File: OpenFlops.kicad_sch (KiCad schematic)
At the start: 87 parts, among them J99 OSHW_LOGO, P1 FLOPPY_CONN, P10 SD CARD, P11 SD PWR, P12 SD_DISABLE, P2 POWER_INPUT, P3 USB_A_FEMALE, P4 PROG_PORT, P5 JUMPER_JC, P6 ENCODER_PORT, P7 DISPLAY_PORT, P8 USB_HEADER, P9 EXTERNAL_SPEAKER, Q1 BSS138, Q2 BSS138, Q3 BSS138, Q4 BSS138, Q5 BSS138, Q6 BSS138, Q7 MMBT3904, U1 74HCT04, U3 STM32F105RBT6, U4 LM1117-3.3, Y1 8 MHz

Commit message: Change C1, C17 and C19 to SMD parts
This commit changes C1, C17 and C19 to SMD electrolytic capacitors. The Panasonic FT series (see https://industrial.panasonic.com/cdbs/www-data/pdf/RDE0000/ABA0000C1240.pdf) has both 10µF and 100µF available with 5x5.8 packages, so these are the used footprints.
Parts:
- C1, C17, C19: footprint Capacitor_THT:CP_Radial_D6.3mm_P2.50mm -> Capacitor_SMD:CP_Elec_5x5.8
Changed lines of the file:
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@@
 			)
 		)
-		(property "Footprint" "Capacitor_THT:CP_Radial_D6.3mm_P2.50mm"
+		(property "Footprint" "Capacitor_SMD:CP_Elec_5x5.8"
 			(at 138.303 56.388 0)
 			(effects
@@
 			)
 		)
-		(property "Description" ""
+		(property "Description" "Panasonic EEEFT1H100AR"
 			(at 138.303 56.388 0)
 			(effects
@@
 			)
 		)
-		(property "Footprint" "Capacitor_THT:CP_Radial_D6.3mm_P2.50mm"
+		(property "Footprint" "Capacitor_SMD:CP_Elec_5x5.8"
 			(at 170.18 56.388 0)
 			(effects
@@
 			)
 		)
-		(property "Description" ""
+		(property "Description" "Panasonic EEEFT1H100AR"
 			(at 170.18 56.388 0)
 			(effects
@@
 			)
 		)
-		(property "Footprint" "Capacitor_THT:CP_Radial_D6.3mm_P2.50mm"
+		(property "Footprint" "Capacitor_SMD:CP_Elec_5x5.8"
 			(at 114.808 55.753 0)
 			(effects
@@
 			)
 		)
-		(property "Description" ""
+		(property "Description" "Panasonic EEEFT1C101AR"
 			(at 114.808 55.753 0)
 			(effects

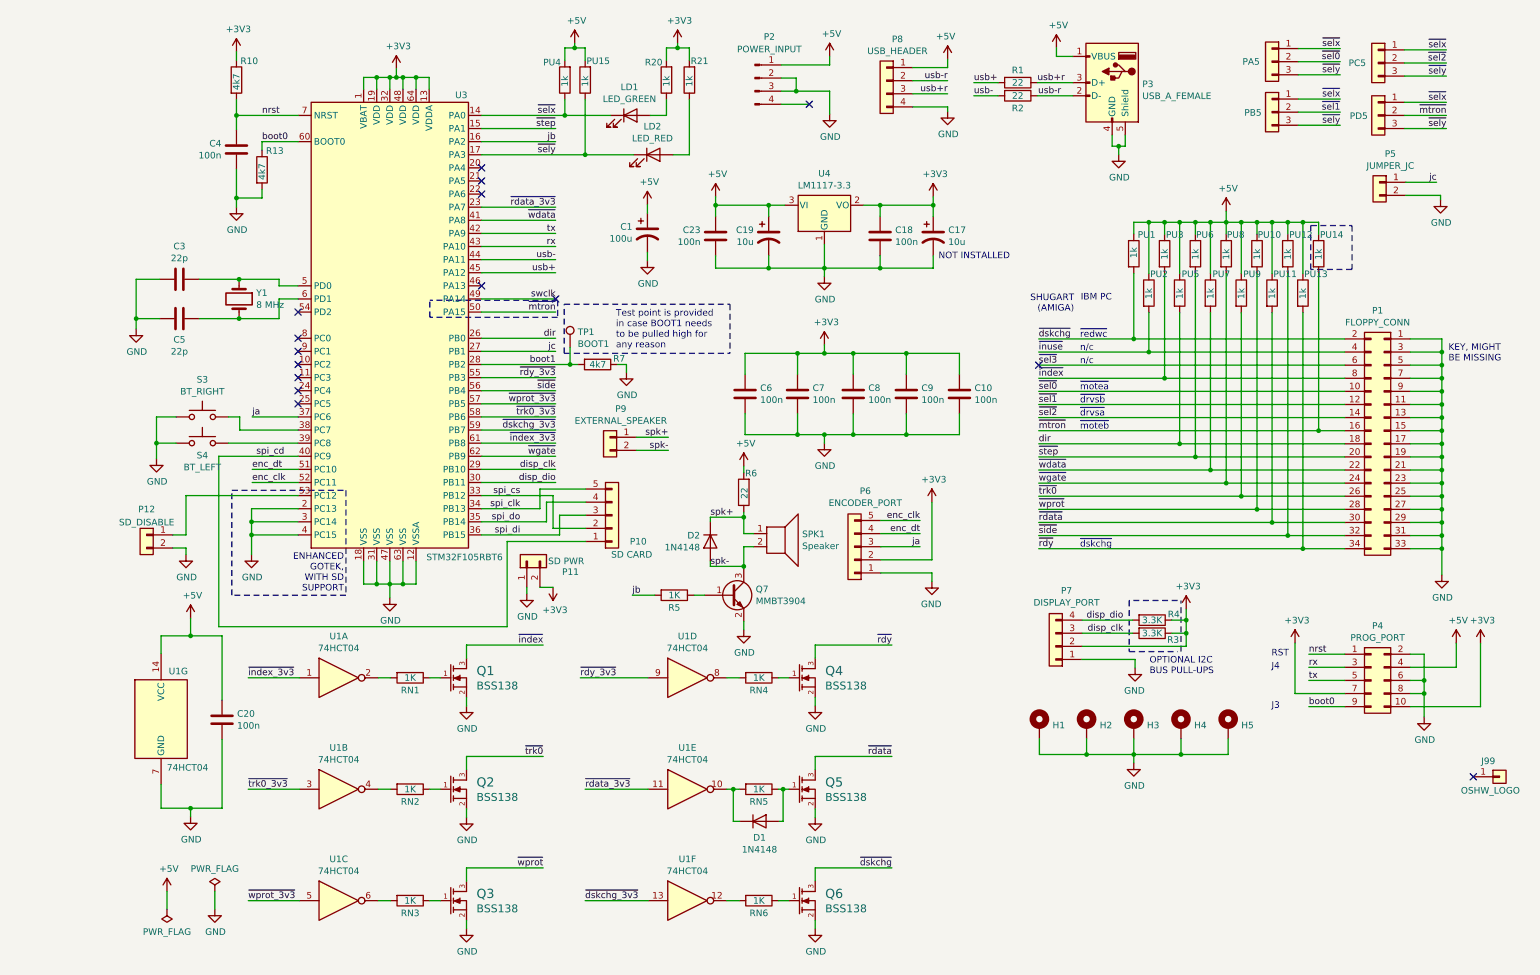
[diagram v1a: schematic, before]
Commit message: Major rerouting Still not completely satisfied though
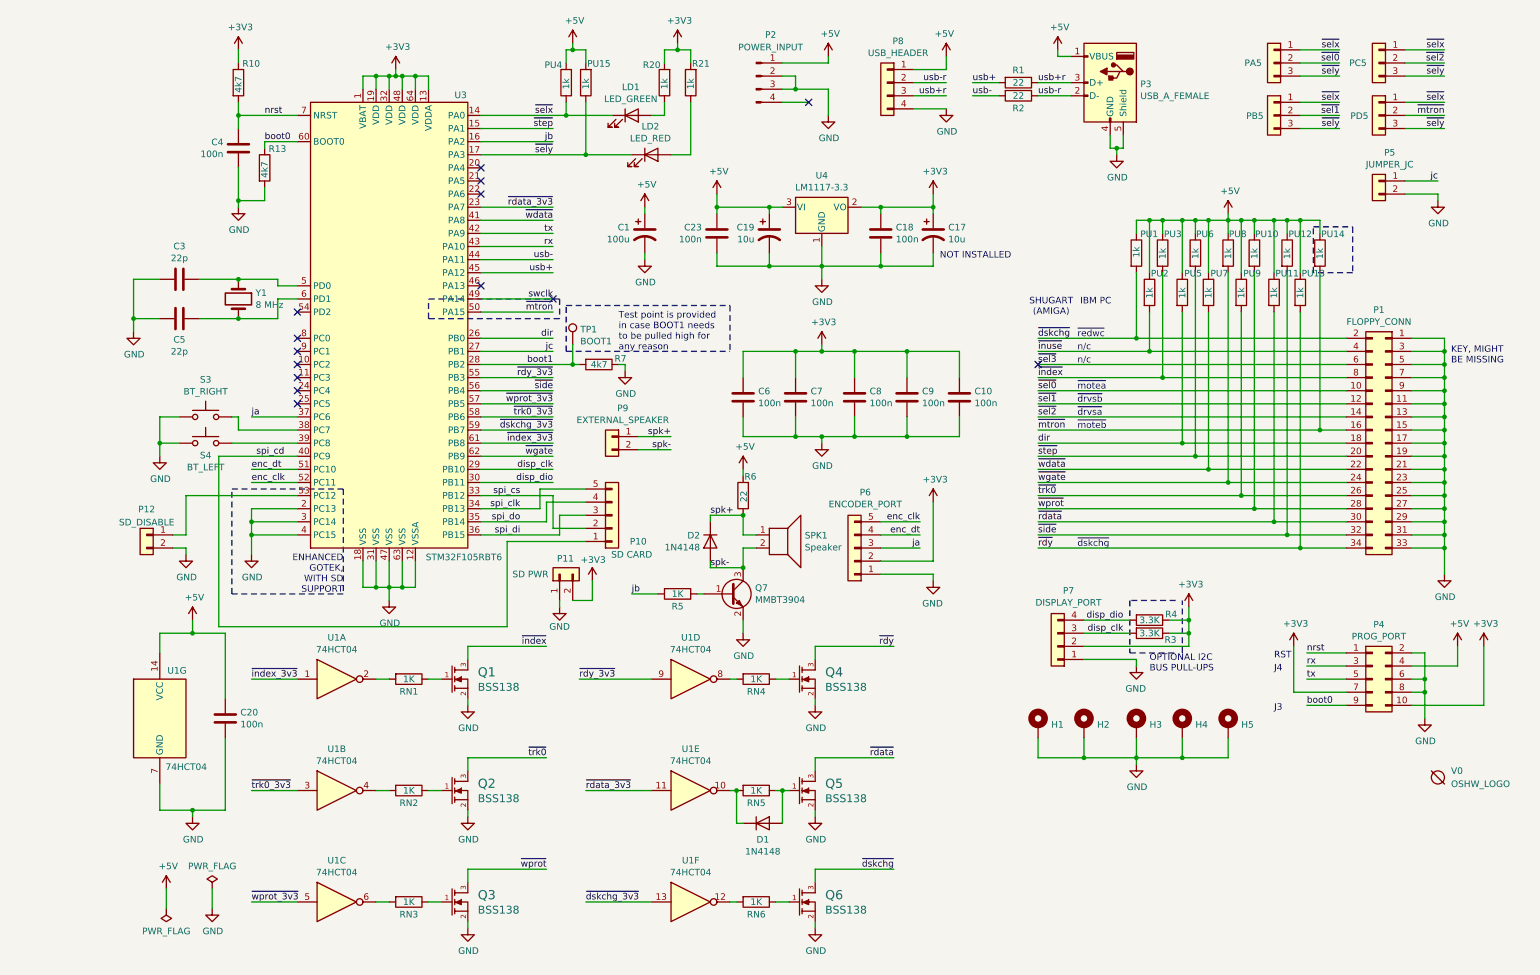
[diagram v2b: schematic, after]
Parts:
- removed J99: OSHW_LOGO, Symbol:OSHW-Logo2_9.8x8mm_Copper, symbol Connector_Generic:Conn_01x01
- added V0: OSHW_LOGO, Symbol:OSHW-Logo2_9.8x8mm_Copper, symbol void:Void
- Q7: footprint Package_TO_SOT_SMD:SOT-23_Handsoldering -> Package_TO_SOT_SMD:SOT-23
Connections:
- no-connect marks 15 -> 14
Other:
- moved on the sheet: C1, C10, C17, C18, C19, C20, C23, C6, C7, C8, C9, D1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

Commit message: Update footprints
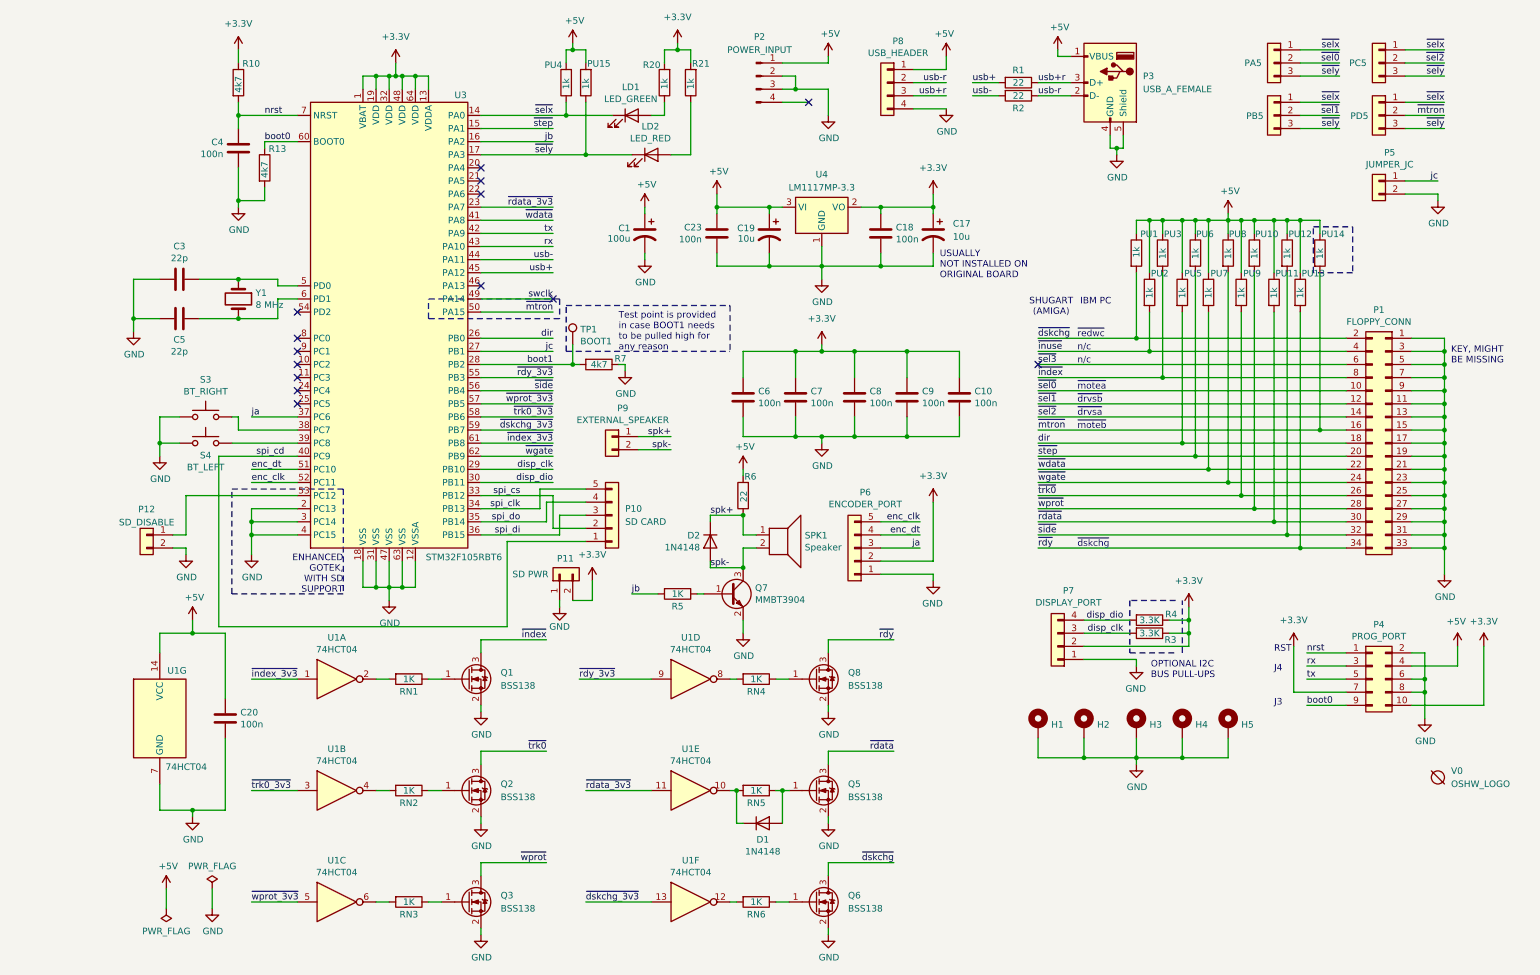
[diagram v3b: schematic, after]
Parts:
- removed C1: 100u, Capacitor_SMD:CP_Elec_5x5.8, symbol OpenFlops-rescue:CP1-Device
- removed C17, C19: 10u, Capacitor_SMD:CP_Elec_5x5.8, symbol OpenFlops-rescue:CP1-Device
- removed P2: POWER_INPUT, OpenFlops:PinHeader_1x04_P2.54mm_Vertical, symbol Connector:Conn_01x04_Male
- removed P3: USB_A_FEMALE, OpenFlops:USB_A_FEMALE, symbol OpenFlops-rescue:USB_A-Connector
- removed Q1, Q2, Q3, Q4, Q5, Q6: BSS138, Package_TO_SOT_SMD:SOT-23_Handsoldering, symbol OpenFlops-rescue:MOS_N_GSD-w_transistor
- removed U4: LM1117-3.3, Package_TO_SOT_SMD:SOT-223-3_TabPin2, symbol Regulator_Linear:LM1117-3.3
- added C1: 100u, Capacitor_SMD:CP_Elec_5x5.8, symbol Device:C_Polarized_US
- added C17, C19: 10u, Capacitor_SMD:CP_Elec_5x5.8, symbol Device:C_Polarized_US
- added P2: POWER_INPUT, Connector_PinHeader_2.54mm:PinHeader_1x04_P2.54mm_Vertical, symbol Connector:Conn_01x04_Pin
- added P3: USB_A_FEMALE, OpenFlops:USB_A_FEMALE, symbol Connector:USB_A
- added Q1, Q2, Q3, Q5, Q6, Q8: BSS138, Package_TO_SOT_SMD:SOT-23, symbol Transistor_FET:BSS138
- added U4: LM1117MP-3.3, Package_TO_SOT_SMD:SOT-223-3_TabPin2, symbol Regulator_Linear:LM1117MP-3.3
- C10, C18, C20, C23, C3, C4, C5, C6, C7, C8, C9: footprint Capacitor_SMD:C_0805_2012Metric_Pad1.15x1.40mm_HandSolder -> Capacitor_SMD:C_0805_2012Metric_Pad1.18x1.45mm_HandSolder
- P10, P6: footprint OpenFlops:PinHeader_1x05_P2.54mm_Vertical -> Connector_PinHeader_2.54mm:PinHeader_1x05_P2.54mm_Vertical
- P11, P12, P5: footprint OpenFlops:PinHeader_1x02_P2.54mm_Vertical -> Connector_PinHeader_2.54mm:PinHeader_1x02_P2.54mm_Vertical
- P4: footprint OpenFlops:PinHeader_2x05_P2.54mm_Vertical -> Connector_PinHeader_2.54mm:PinHeader_2x05_P2.54mm_Vertical
- P7, P8: footprint OpenFlops:PinHeader_1x04_P2.54mm_Vertical -> Connector_PinHeader_2.54mm:PinHeader_1x04_P2.54mm_Vertical
- PU1, PU10, PU11, PU12, PU13, PU14, PU15, PU2, PU3, PU4, PU5, PU6, PU7, PU8, PU9, R1, R10, R13, R2, R20, R21, R3, R4, R5, R6, R7, RN1, RN2, RN3, RN4, RN5, RN6: footprint Resistor_SMD:R_0805_2012Metric_Pad1.15x1.40mm_HandSolder -> Resistor_SMD:R_0805_2012Metric_Pad1.20x1.40mm_HandSolder
- V0: footprint Symbol:OSHW-Logo2_9.8x8mm_Copper -> Symbol:OSHW-Logo2_7.3x6mm_Copper
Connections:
- net +5V: now also C1.1, C19.1, P2.1 (Pin_1), P3.1 (VBUS), U4.3 (VI)
- net GND: now also C1.2, C17.2, C19.2, P2.2 (Pin_2), P2.3 (Pin_3), P3.4 (GND), P3.5 (Shield), Q1.2 (S), Q2.2 (S), Q3.2 (S), Q5.2 (S), Q6.2 (S), Q8.2 (S), U4.1 (GND)
- net usb+r: now also P3.3 (D+)
- net usb-r: now also P3.2 (D-)
- net ~{dskchg}: now also Q6.3 (D)
- net ~{index}: now also Q1.3 (D)
- net ~{rdata}: now also Q5.3 (D)
- net ~{rdy}: now also Q8.3 (D)
- net ~{trk0}: now also Q2.3 (D)
- net ~{wprot}: now also Q3.3 (D)
- net at RN1.1: now also Q1.1 (G)
- net at RN2.1: now also Q2.1 (G)
- net at RN3.1: now also Q3.1 (G)
- net at RN4.1: now also Q8.1 (G)
- net at D1.2 (A), RN5.1: now also Q5.1 (G)
- net at RN6.1: now also Q6.1 (G)
- net +3V3 renamed +3.3V
- net +3.3V: now also C17.1, U4.2 (VO)
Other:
- note added: "USUALLY NOT INSTALLED ON ORIGINAL BOARD"
- note removed: "NOT INSTALLED"

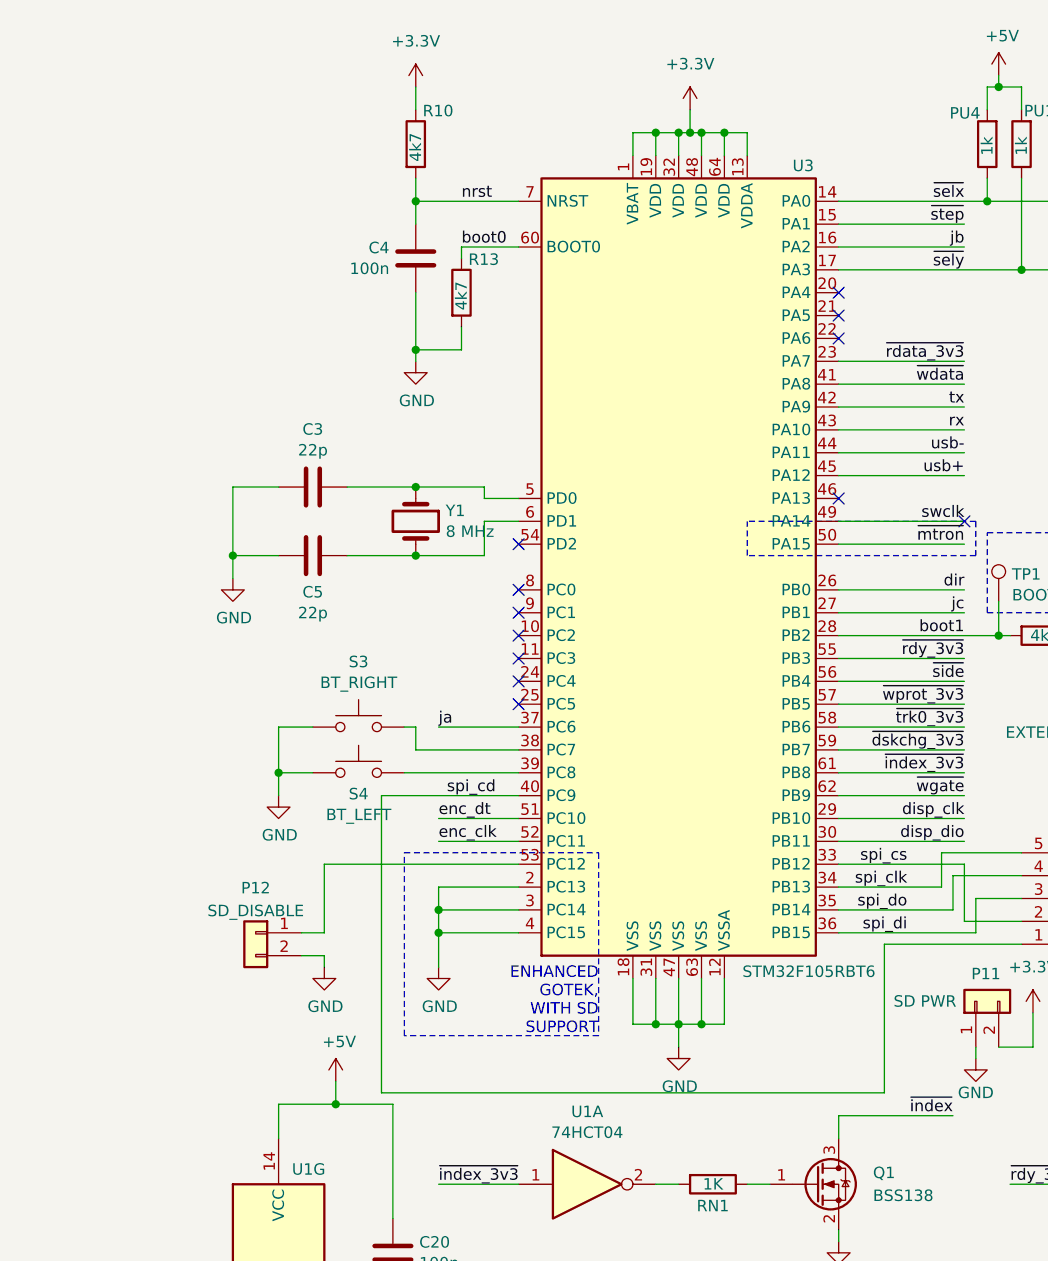
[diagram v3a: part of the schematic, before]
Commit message: Update MCU footprint MCU and MOSFET are no longer "handsolder", not sure if it's OK...
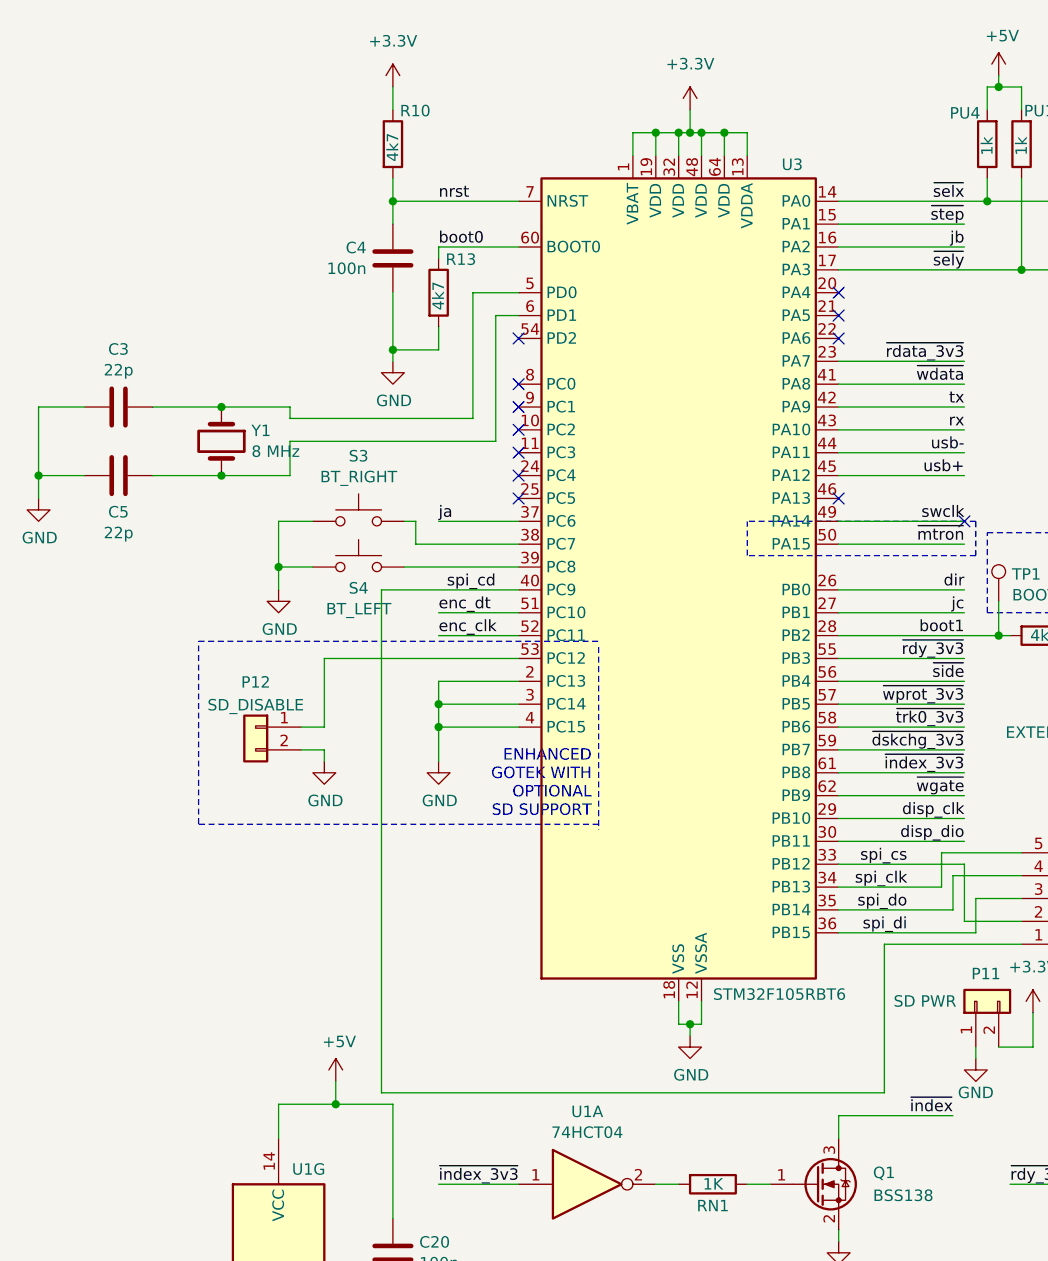
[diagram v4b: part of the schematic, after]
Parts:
- U3: footprint OpenFlops:LQFP-64_Handsoldering -> Package_QFP:LQFP-64_10x10mm_P0.5mm; JLCPCB PN STM32F105RBT6 -> (none); MFG Name STMICROELECTRONICS -> (none); MFG Part Num ST MICROELECTRONICS LQFP-64_10X10X05P ROHS Extended Part -> (none)
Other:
- note added: "ENHANCED GOTEK WITH OPTIONAL SD SUPPORT"
- note removed: "ENHANCED GOTEK, WITH SD SUPPORT"
- moved on the sheet: C3, C4, C5, P12, R10, R13, S3, S4, Y1

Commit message: Switch crystal to SMD
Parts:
- Y1: footprint Crystal:Crystal_HC49-U_Vertical -> Crystal:Crystal_SMD_HC49-SD
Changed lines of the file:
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@@
 			)
 		)
-		(property "Footprint" "Crystal:Crystal_HC49-U_Vertical"
+		(property "Footprint" "Crystal:Crystal_SMD_HC49-SD"
 			(at 13.97 59.69 0)
 			(effects
